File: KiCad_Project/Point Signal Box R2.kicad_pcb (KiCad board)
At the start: 2 copper layers, 47.8 x 47.2 mm, 36 parts, among them J1 Alternate DCC, J2 SPDT on PM1, J3 SPDT on PM2, M3 MountingHole_3.2mm_M3_DIN965_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, U1 TLP241B, U2 TLP241B, U3 TLP241B, U4 TLP241B

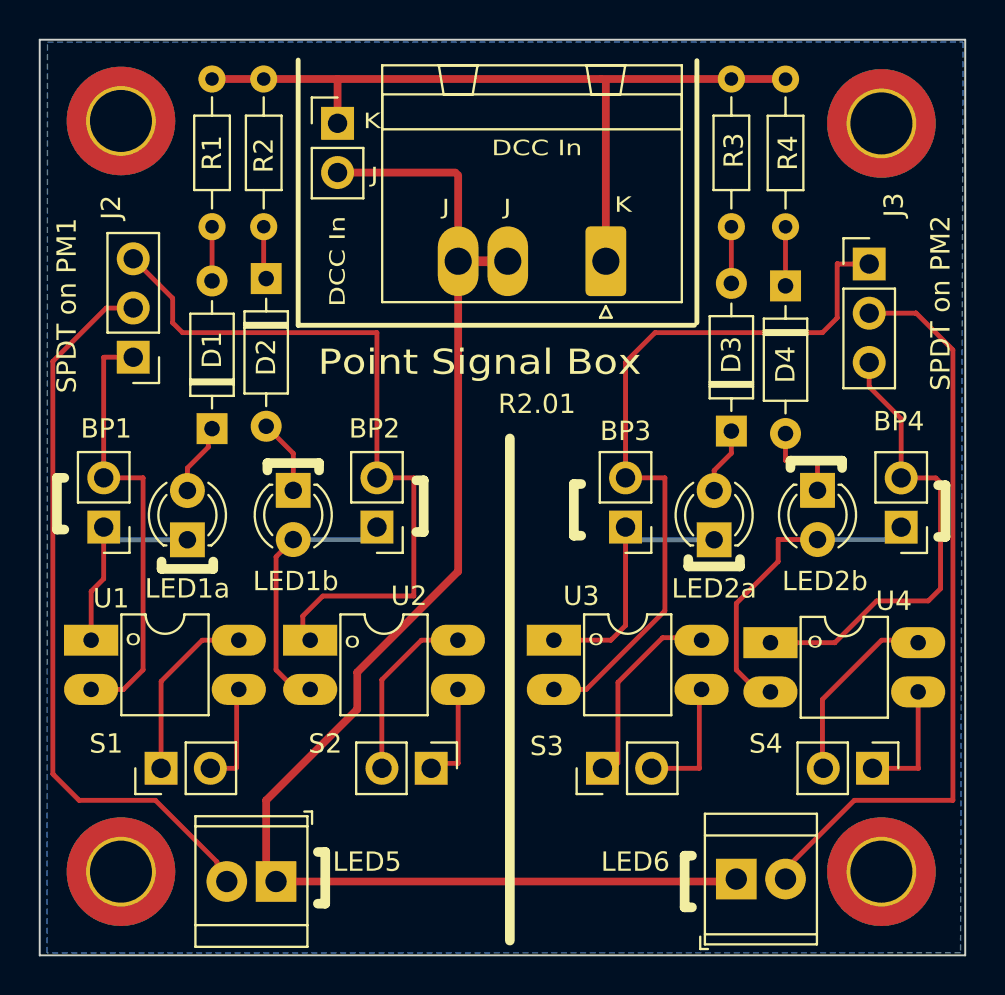
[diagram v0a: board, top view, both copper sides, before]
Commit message: Removed KiCad backups
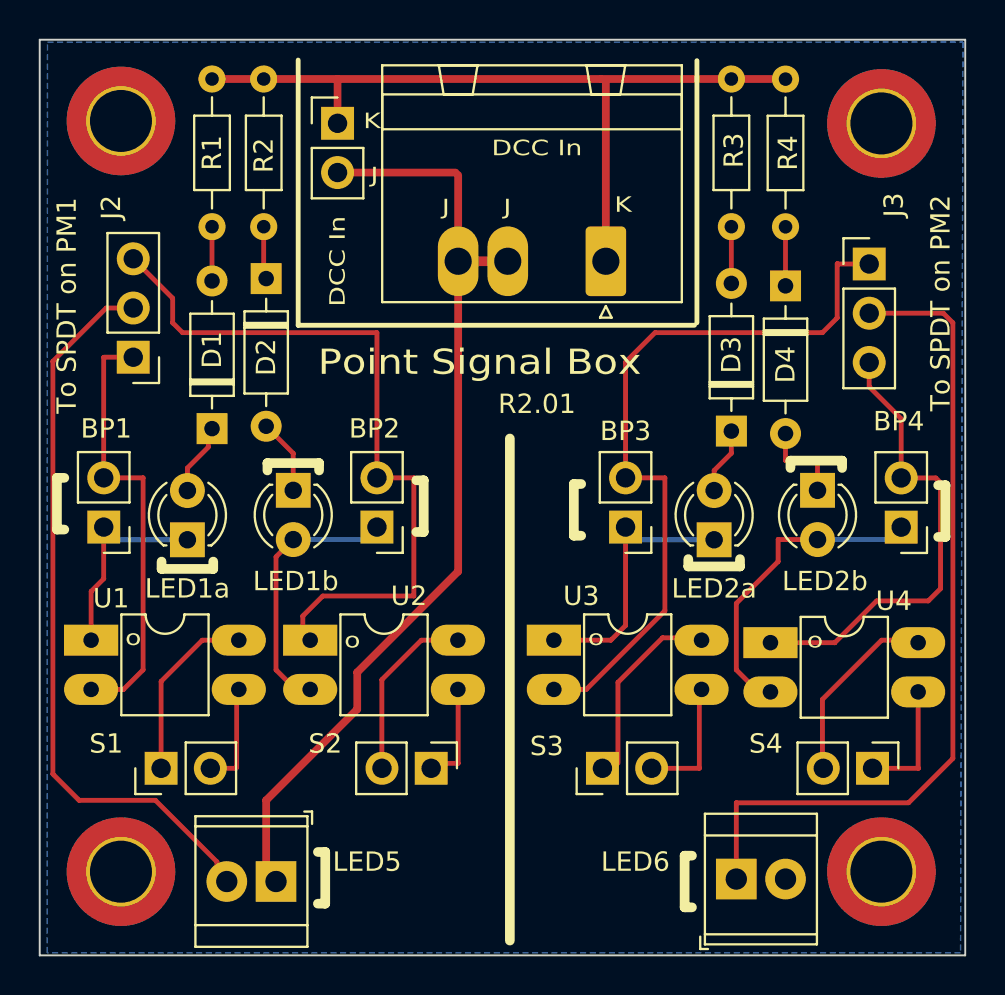
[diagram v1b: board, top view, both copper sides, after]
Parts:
- J2: value SPDT on PM1 -> To SPDT on PM1
- J3: value SPDT on PM2 -> To SPDT on PM2
- LED5, LED6: value To Signal -> To Signal LED
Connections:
- LED6 pad 1: DCCJ -> Net-(J3-Pad2)
- LED6 pad 2: Net-(J3-Pad2) -> DCCJ
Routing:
- net DCCJ: track 73.1 -> 49.4 mm
- net Net-(J3-Pad2): track 39.2 -> 43.1 mm
- net Net-(BP4-Pad1): track 15.6 -> 14.9 mm
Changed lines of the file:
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@@
       (effects (font (size 1 1) (thickness 0.15)))
     )
-    (fp_text value "SPDT on PM2" (at 3.683 2.017 90) (layer "F.SilkS")
+    (fp_text value "To SPDT on PM2" (at 3.683 2.017 90) (layer "F.SilkS")
       (effects (font (size 1 1) (thickness 0.15)))
     )
@@
       (effects (font (size 1 1) (thickness 0.15)))
     )
-    (fp_text value "To Signal" (at -5.842 -0.889) (layer "F.Fab")
+    (fp_text value "To Signal LED" (at -5.842 -0.889) (layer "F.Fab")
       (effects (font (size 1 0.8) (thickness 0.15)))
     )
@@
       (effects (font (size 1 1) (thickness 0.15)))
     )
-    (fp_text value "SPDT on PM1" (at 3.429 2.667 90) (layer "F.SilkS")
+    (fp_text value "To SPDT on PM1" (at 3.429 2.667 90) (layer "F.SilkS")
       (effects (font (size 1 1) (thickness 0.15)))
     )
@@
       (effects (font (size 1 1) (thickness 0.15)))
     )
-    (fp_text value "To Signal" (at -6.096 0.889) (layer "F.Fab")
+    (fp_text value "To Signal LED" (at -6.096 0.889) (layer "F.Fab")
       (effects (font (size 1 0.8) (thickness 0.15)))
     )
@@
     (fp_circle (center 2.54 0) (end 3.64 0) (layer "F.Fab") (width 0.1) (fill none))
     (pad "1" thru_hole rect (at 0 0) (size 2.1 2.1) (drill 1.1) (layers *.Cu *.Mask)
-      (net 4 "DCCJ") (pinfunction "Pin_1") (pintype "passive"))
+      (net 13 "Net-(J3-Pad2)") (pinfunction "Pin_1") (pintype "passive"))
     (pad "2" thru_hole circle (at 2.54 0) (size 2.1 2.1) (drill 1.1) (layers *.Cu *.Mask)
-      (net 13 "Net-(J3-Pad2)") (pinfunction "Pin_2") (pintype "passive"))
+      (net 4 "DCCJ") (pinfunction "Pin_2") (pintype "passive"))
     (model "${KICAD6_3DMODEL_DIR}/TerminalBlock_TE-Connectivity.3dshapes/TerminalBlock_TE_282834-2_1x02_P2.54mm_Horizontal.wrl"
       (offset (xyz 0 0 0))
@@
   (segment (start 125.857 74.681) (end 127.254 76.078) (width 0.25) (layer "F.Cu") (net 3))
   (segment (start 135.763 82.169) (end 135.763 66.167) (width 0.4) (layer "F.Cu") (net 4))
-  (segment (start 149.601 98.171) (end 125.857 98.171) (width 0.4) (layer "F.Cu") (net 4))
   (segment (start 135.763 66.167) (end 135.763 61.722) (width 0.4) (layer "F.Cu") (net 4))
   (segment (start 135.631 61.59) (end 129.54 61.59) (width 0.4) (layer "F.Cu") (net 4))
@@
   (segment (start 131.572 69.85) (end 131.572 77.343) (width 0.25) (layer "F.Cu") (net 12))
   (segment (start 128.778 83.439) (end 133.477 83.439) (width 0.25) (layer "F.Cu") (net 12))
-  (segment (start 152.141 98.044) (end 156.205 93.98) (width 0.25) (layer "F.Cu") (net 13))
-  (segment (start 161.29 70.739) (end 159.385 68.834) (width 0.25) (layer "F.Cu") (net 13))
-  (segment (start 156.205 93.98) (end 161.29 93.98) (width 0.25) (layer "F.Cu") (net 13))
-  (segment (start 159.37 68.849) (end 156.972 68.849) (width 0.25) (layer "F.Cu") (net 13))
-  (segment (start 161.29 93.98) (end 161.29 70.739) (width 0.25) (layer "F.Cu") (net 13))
-  (segment (start 159.385 68.834) (end 159.37 68.849) (width 0.25) (layer "F.Cu") (net 13))
+  (segment (start 161.29 69.342) (end 161.29 91.821) (width 0.25) (layer "F.Cu") (net 13))
+  (segment (start 160.797 68.849) (end 161.29 69.342) (width 0.25) (layer "F.Cu") (net 13))
+  (segment (start 159.004 94.107) (end 150.114 94.107) (width 0.25) (layer "F.Cu") (net 13))
+  (segment (start 161.29 91.821) (end 159.004 94.107) (width 0.25) (layer "F.Cu") (net 13))
+  (segment (start 156.972 68.849) (end 160.797 68.849) (width 0.25) (layer "F.Cu") (net 13))
+  (segment (start 150.114 94.107) (end 150.114 98.044) (width 0.25) (layer "F.Cu") (net 13))
   (segment (start 126.365 87.249) (end 127.376 88.26) (width 0.25) (layer "F.Cu") (net 14))
   (segment (start 127.254 80.528) (end 126.365 81.417) (width 0.25) (layer "F.Cu") (net 14))
@@
   (segment (start 156.972 71.389) (end 156.972 72.644) (width 0.25) (layer "F.Cu") (net 27))
   (segment (start 150.114 83.82) (end 152.273 81.661) (width 0.25) (layer "F.Cu") (net 28))
-  (segment (start 151.877 88.387) (end 151.252 88.387) (width 0.25) (layer "F.Cu") (net 28))
   (segment (start 152.273 81.661) (end 152.273 80.518) (width 0.25) (layer "F.Cu") (net 28))
   (segment (start 152.283 80.528) (end 154.305 80.528) (width 0.25) (layer "F.Cu") (net 28))
